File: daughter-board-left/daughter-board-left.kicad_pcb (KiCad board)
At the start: 2 copper layers, 40 x 30 mm, 20 parts, among them J1 Conn_01x06_MountingPin, J2 USB_C_Receptacle_USB2.0_16P, J3 PJ-320A, U1 SRV05-4

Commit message: quick save
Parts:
- J1: footprint Connector_JST:JST_SHL_SM06B-SHLS-TF_1x06-1MP_P1.00mm_Horizontal -> Connector_JST:JST_SH_SM06B-SRSS-TB_1x06-1MP_P1.00mm_Horizontal
- moved C4 6.00 mm to (105.2, 75.5)
- moved C5 6.00 mm to (137.2, 75.5)
- moved H3 6.00 mm to (104.0, 80.0)
- moved H4 6.00 mm to (136.0, 80.0)
- moved R6 6.00 mm to (102.8, 75.5)
- moved R7 6.00 mm to (134.8, 75.5)
- moved J1 5.50 mm to (120.0, 80.0)
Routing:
- net /SPLIT_RX: track 24.0 -> 18.2 mm
- net /USB_D-: track 23.8 -> 20.0 mm
- net /USB_D+: track 24.1 -> 20.5 mm
- net +5V: track 49.5 -> 46.6 mm
- net /SPLIT_TX: track 20.9 -> 18.5 mm
- net GND: vias 37 -> 32
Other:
- board size 40 x 30 mm -> 40 x 24 mm

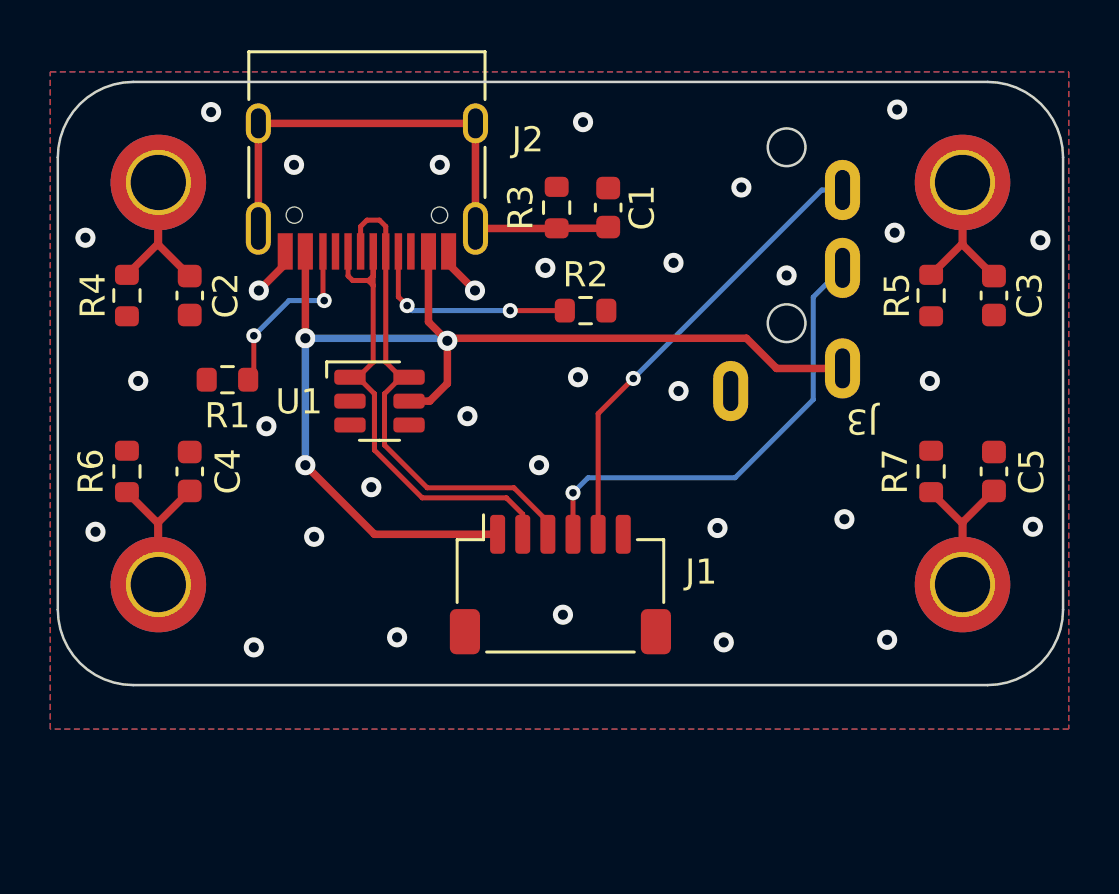
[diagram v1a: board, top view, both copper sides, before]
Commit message: finalised first version of pcbs for prototype order added openscad file for the left halfs case
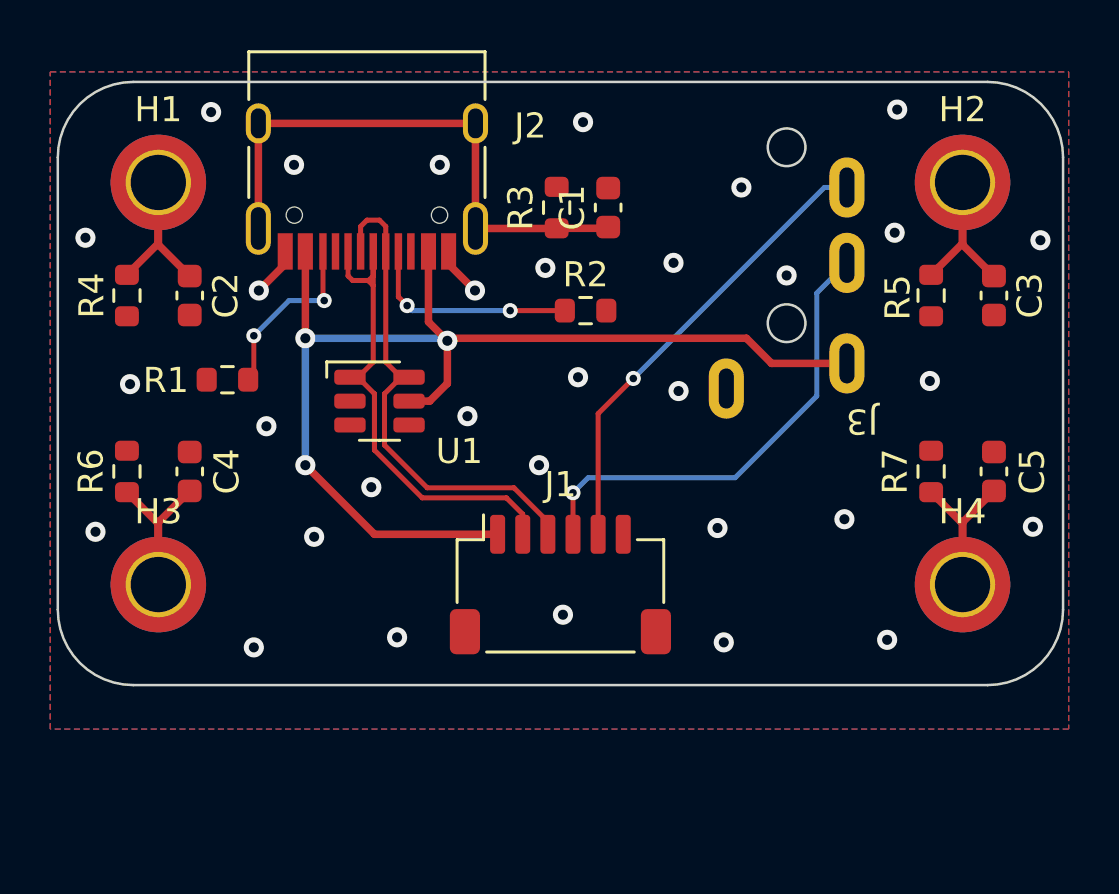
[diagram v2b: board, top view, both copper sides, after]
